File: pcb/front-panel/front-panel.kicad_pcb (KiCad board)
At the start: 2 copper layers, 99.1 x 19 mm, 5 parts, among them J1 HEADER-1x05, U1 ER-OLED1602-4W, U2 TSL2561

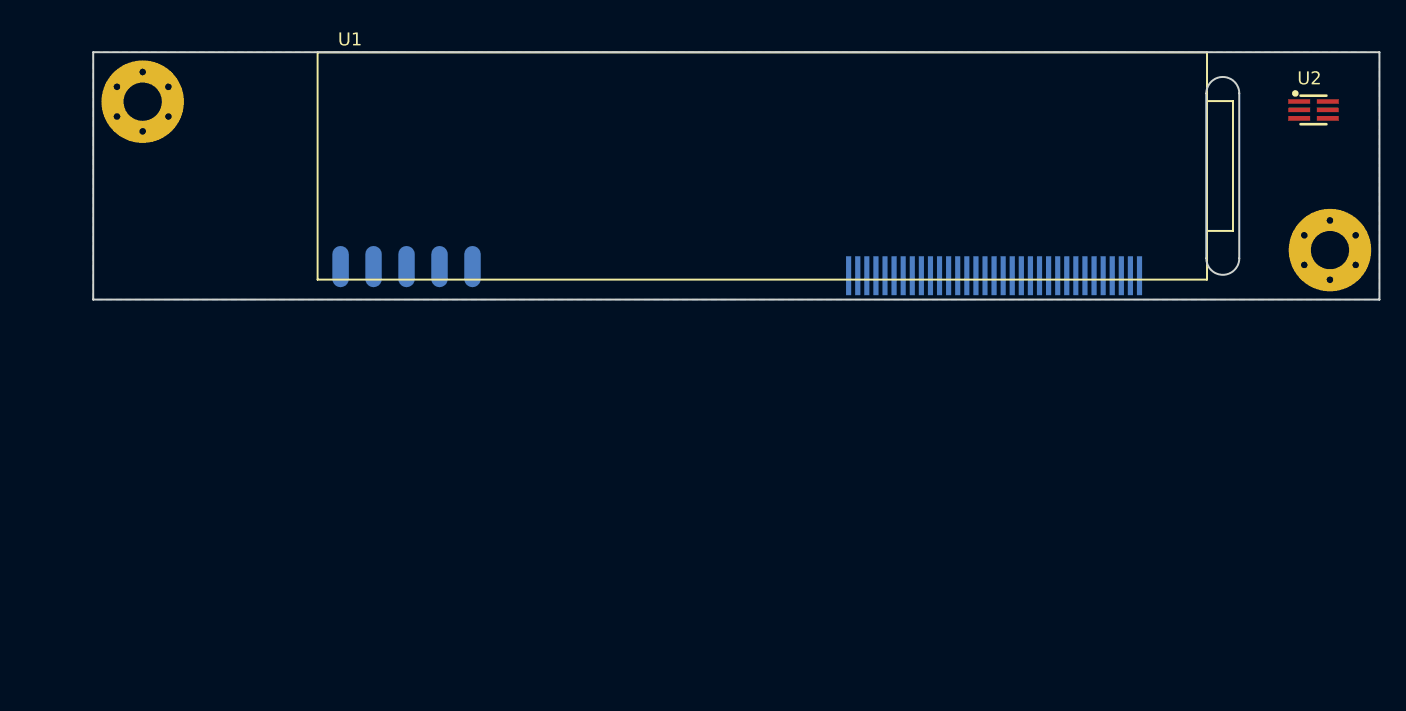
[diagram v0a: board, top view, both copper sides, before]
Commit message: Added schematic for front panel pcb
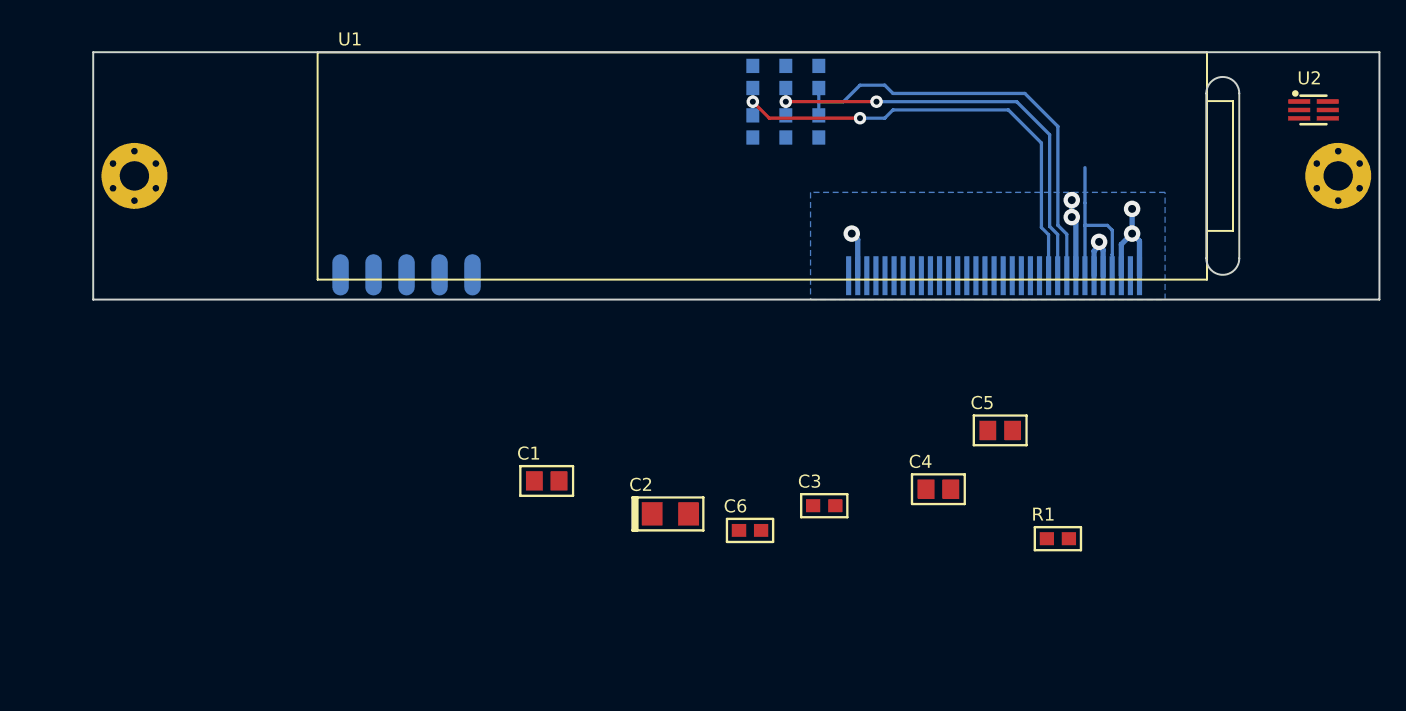
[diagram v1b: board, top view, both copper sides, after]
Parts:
- removed REF (x2): Hole-Screw-#4, Conn-Wire-Pads:Hole-Screw-#4
- added C1: 1uF, SMT:C-0805, F.Cu at (129.5, 128.3)
- added C2: 4.7uF, SMT:CPL-1206, F.Cu at (139.1, 130.8)
- added C3: 100nF, SMT:C-0603, F.Cu at (150.9, 130.2)
- added C4: 10uF, SMT:C-0805, F.Cu at (159.7, 128.9)
- added C5: 10uF, SMT:C-0805, F.Cu at (164.5, 124.4)
- added C6: 100nF, SMT:C-0603, F.Cu at (145.2, 132.1)
- added H1: Hole, Conn-Wire-Pads:Hole-Screw-#2, F.Cu at (190.5, 104.8)
- added H2: Hole, Conn-Wire-Pads:Hole-Screw-#2, F.Cu at (97.8, 104.8)
- added R1: 500k, SMT:R-0603, F.Cu at (168.9, 132.7)
- added R2: N/A, SMT:R-0603, B.Cu at (150.5, 97.2)
- added R3: 0, SMT:R-0603, B.Cu at (150.5, 101.0)
- added R4: 0, SMT:R-0603, B.Cu at (148.0, 97.2)
- added R5: N/A, SMT:R-0603, B.Cu at (148.0, 101.0)
- added R6: N/A, SMT:R-0603, B.Cu at (145.4, 97.2)
- added R7: 0, SMT:R-0603, B.Cu at (145.4, 101.0)
- moved J1 0.63 mm to (118.7, 112.4)
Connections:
- net Net-(U1-Pad12) renamed /VCC_EN
- J1 pad 1: +3V3 -> +5V
- U1 pad 10: +3V3 -> Net-(R4-Pad2)
- U1 pad 11: GND -> Net-(R6-Pad2)
- U1 pad 14: Net-(U1-Pad14) -> /RESET
- U1 pad 32: Net-(U1-Pad32) -> +12V
- U1 pad 4: Net-(U1-Pad4) -> Net-(C1-Pad2)
- U1 pad 5: Net-(U1-Pad5) -> +5V
- U1 pad 6: +3V3 -> +5V
- U1 pad 7: Net-(U1-Pad7) -> Net-(C1-Pad2)
- U1 pad 8: Net-(U1-Pad8) -> +5V
- U1 pad 9: GND -> Net-(R2-Pad2)
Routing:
- net Net-(R6-Pad2): track 0.00 -> 36.6 mm, vias 0 -> 2
- net Net-(R4-Pad2): track 0.00 -> 34.6 mm, vias 0 -> 2
- net Net-(R2-Pad2): track 0.00 -> 34.1 mm
- net Net-(C1-Pad2): track 0.00 -> 14.1 mm
- net +5V: track 0.00 -> 11.1 mm, vias 0 -> 3
- net GND: track 0.00 -> 8.97 mm, vias 0 -> 2
- net +12V: track 0.00 -> 3.43 mm, vias 0 -> 1
- added copper zone on Power, net +5V
- added copper zone on GND, net GND
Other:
- copper layers 2 -> 4
- net class Default: clearance 0.2 -> 0.254; trace_width 0.25 -> 0.254; via_dia 0.6 -> 0.9652; via_drill 0.4 -> 0.4572
- net class Power added: clearance 0.254, trace_width 0.4064, via_dia 1.27, via_drill 0.6096
- rule trace_clearance: 0.2 -> 0.254

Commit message: Added front panel pcb
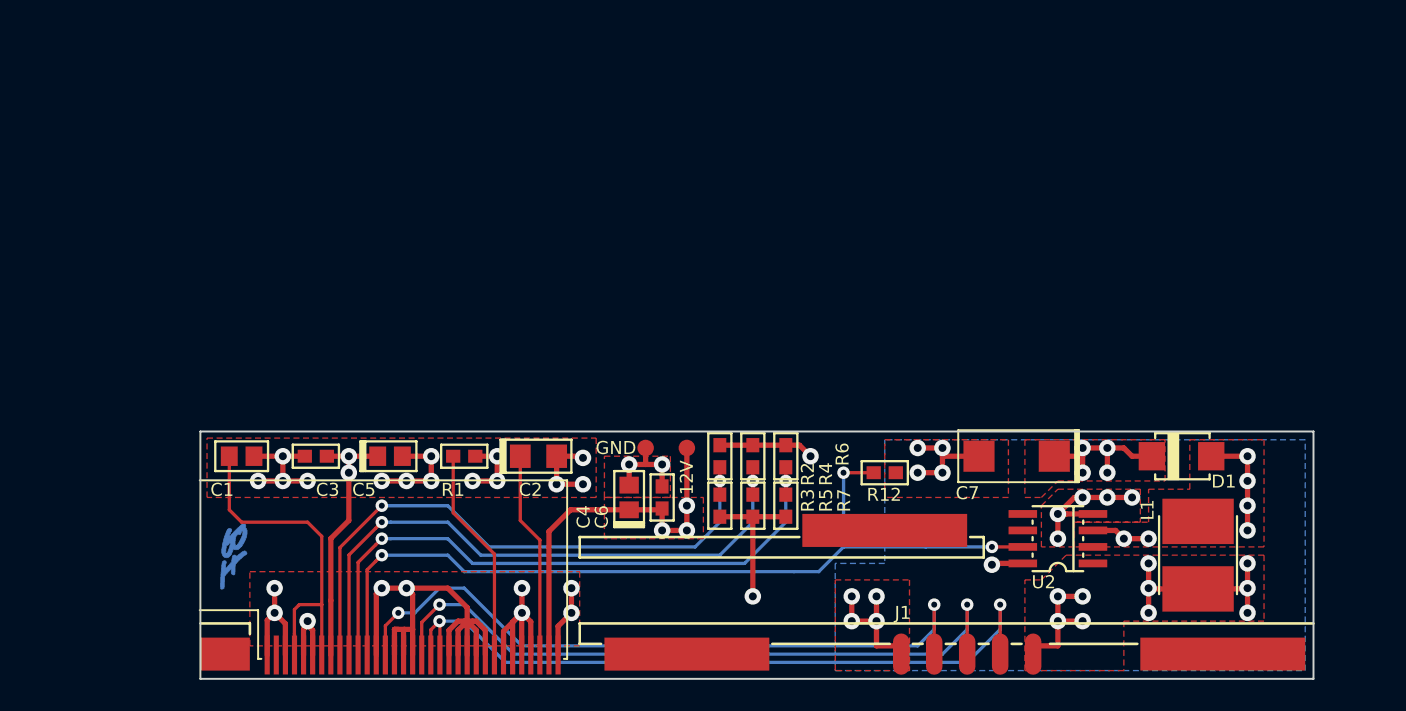
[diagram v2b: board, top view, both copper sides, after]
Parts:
- removed H1, H2: Hole, Conn-Wire-Pads:Hole-Screw-#2
- added C7: 22uF, SMT:CPL-2312, F.Cu at (165.7, 126.4)
- added D1: MBRS120T3, SMT:DO-214-AA, F.Cu at (178.4, 126.4)
- added J2: HEADER-1x01, Conn-Wire-Pads:SolderPad-100x500, F.Cu at (181.6, 141.6)
- added J3: HEADER-1x01, Conn-Wire-Pads:SolderPad-100x500, F.Cu at (140.3, 141.6)
- added J4: HEADER-1x01, Conn-Wire-Pads:SolderPad-100x500, F.Cu at (155.6, 132.1)
- added J5: HEADER-1x01, Conn-Wire-Pads:SolderPad-100x150, F.Cu at (104.8, 141.6)
- added L1: 33uH, SMT:IND-CD54, F.Cu at (179.7, 134.0)
- added R12: 10k, SMT:R-0603, F.Cu at (155.6, 127.6)
- added REF**: VAL**, Symbols:Gauge-X-100mm, B.Cu at (96.5, 143.5)
- added REF**: VAL**, Symbols:SIGNATURE, B.Cu at (105.4, 134.0)
- added REF**: VAL**, Symbols:LOGO-OSHW-150, B.Cu at (179.3, 127.6)
- added REF**: VAL**, Symbols:Gauge-X-100mm, F.Cu at (102.9, 149.9)
- added TP1: 12V, Conn-Wire-Pads:TEST-POINT-50, F.Cu at (140.3, 125.7)
- added TP2: GND, Conn-Wire-Pads:TEST-POINT-50, F.Cu at (137.2, 125.7)
- C4, C5: footprint SMT:C-0805 -> SMT:CPL-0805
- J1, R3, R4, R7: moved to F.Cu
- R2, R5, R6: value N/A -> DNP; moved to F.Cu
- U1: moved to B.Cu
- U2: value TSL2561 -> LT1109CS8-12; footprint SMT-DFN:6 -> SMT-SOIC:SOIC8
- moved J1 52.1 mm to (161.9, 141.6), turned to 180 degrees
- moved C5 47.0 mm to (117.5, 126.4)
- moved R1 46.2 mm to (123.2, 126.4)
- moved C3 39.3 mm to (111.8, 126.4)
- moved U2 38.4 mm to (168.9, 132.7), turned to 90 degrees
- moved R3 30.2 mm to (142.9, 130.2)
- moved R2 30.2 mm to (142.9, 126.4)
- moved U1 29.6 mm to (139.1, 133.2), turned to 180 degrees
- moved R5 29.3 mm to (145.4, 130.2)
- moved R7 29.3 mm to (148.0, 130.2)
- moved R4 29.3 mm to (145.4, 126.4)
- moved R6 29.3 mm to (148.0, 126.4)
- moved C4 23.8 mm to (135.9, 129.5), turned to 90 degrees
- moved C1 23.6 mm to (106.0, 126.4), turned to 180 degrees
- moved C2 11.1 mm to (128.9, 126.4)
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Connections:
- U1 pad 15: (no net) -> GND
- U2 pad 1: (no net) -> +5V
- U2 pad 2: (no net) -> Net-(U2-Pad2)
- U2 pad 3: (no net) -> /SW_12V
- U2 pad 4: (no net) -> GND
- U2 pad 5: (no net) -> Net-(U2-Pad5)
- U2 pad 6: (no net) -> Net-(U2-Pad6)
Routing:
- net GND: track 8.97 -> 148.0 mm, vias 2 -> 38
- net /VCC_EN: track 0.00 -> 66.9 mm, vias 0 -> 3
- net /SDA: track 0.00 -> 56.1 mm, vias 0 -> 2
- net +12V: track 3.43 -> 56.8 mm, vias 1 -> 8
- net /RESET: track 0.00 -> 53.2 mm, vias 0 -> 2
- net /SCL: track 0.00 -> 52.5 mm, vias 0 -> 2
- net +5V: track 11.1 -> 57.1 mm, vias 3 -> 14
- net Net-(R1-Pad1): track 0.00 -> 16.6 mm
- net Net-(C2-PadA): track 0.00 -> 15.9 mm
- net /SW_12V: track 0.00 -> 13.1 mm, vias 0 -> 6
- net Net-(C1-Pad2): track 14.1 -> 27.0 mm
- net Net-(R4-Pad2): track 34.6 -> 47.2 mm
- net Net-(R2-Pad2): track 34.1 -> 46.3 mm, vias 0 -> 2
- net Net-(R6-Pad2): track 36.6 -> 48.2 mm
- added copper zone on F.Cu, net +12V
- added copper zone on Power, net +12V
- added copper zone on F.Cu, net +5V
- added copper zone on F.Cu, net /SW_12V
- added copper zone on Power, net /SW_12V
- added copper zone on F.Cu, net GND
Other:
- board size 99.1 x 19 mm -> 85.7 x 19 mm
- board text added: "PC-04"
- board text added: "REV. A"

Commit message: EN of 12V suply controlled from MCU instead of LCD GPIO
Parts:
- J1: value HEADER-1x05 -> HEADER-1x06; footprint Conn-Wire-Pads:WP-50mil-1x05 -> Conn-Wire-Pads:WP-50mil-1x06
- moved J1 1.42 mm to (160.7, 141.0)
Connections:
- J1 pad 5: GND -> /VCC_EN
- U1 pad 12: /VCC_EN -> Net-(U1-Pad12)
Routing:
- net /VCC_EN: track 66.9 -> 28.0 mm

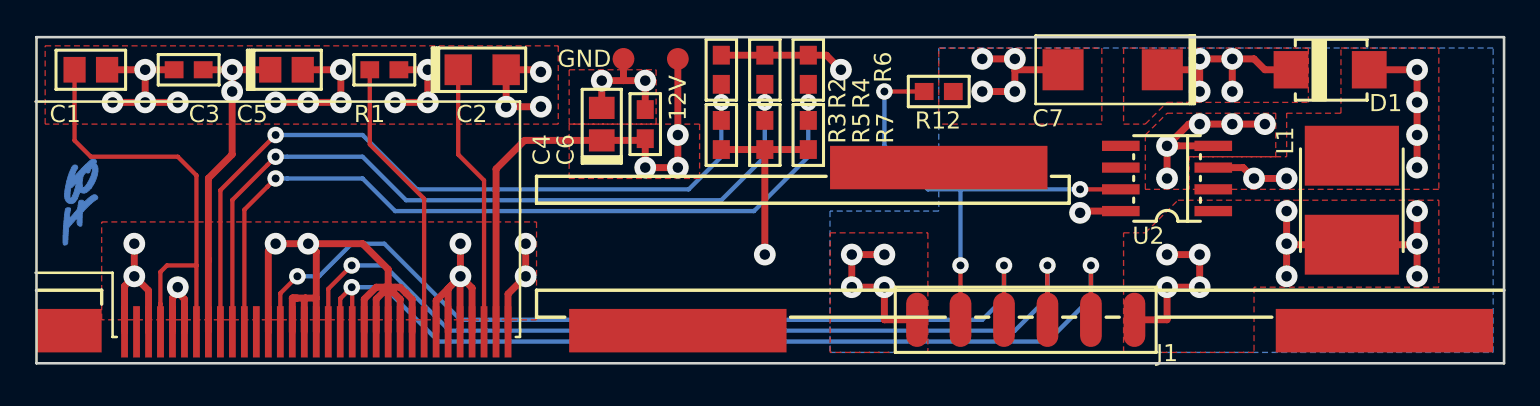
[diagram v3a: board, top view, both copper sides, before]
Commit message: Changed touch keypad, front panel and light sensor pcb to a two layer design.
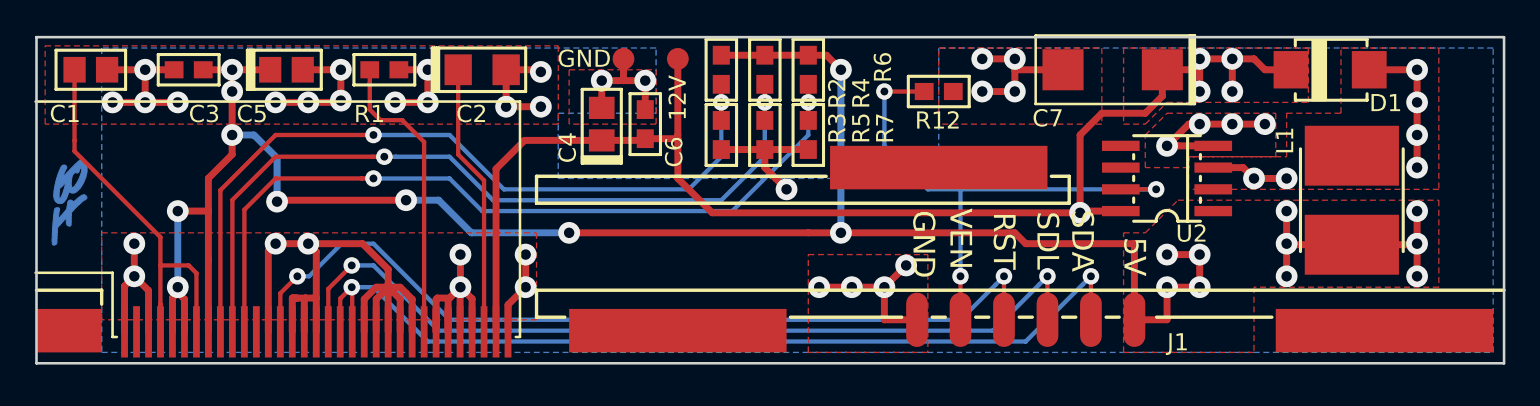
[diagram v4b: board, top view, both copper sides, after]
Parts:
- moved REF** 0.63 mm to (104.8, 134.0)
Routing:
- net +5V: track 57.1 -> 134.2 mm, vias 14 -> 20
- net +12V: track 56.8 -> 78.0 mm, vias 8 -> 5
- net GND: track 148.0 -> 142.6 mm, vias 38 -> 37
- net /VCC_EN: track 28.0 -> 32.1 mm
- net Net-(C1-Pad2): track 27.0 -> 23.1 mm
- net /SDA: track 56.1 -> 54.1 mm
- net /SCL: track 52.5 -> 50.5 mm
- net /RESET: track 53.2 -> 51.2 mm
- net Net-(R1-Pad1): track 16.6 -> 17.4 mm
- net Net-(R6-Pad2): track 48.2 -> 47.5 mm
- removed copper zone on Power, net +12V
- removed copper zone on Power, net +5V
- removed copper zone on Power, net /SW_12V
- removed copper zone on GND, net GND
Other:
- copper layers 4 -> 2
- board text added: "5V"
- board text added: "GND"
- board text added: "RST"
- board text added: "SDA"
- board text added: "SDL"
- board text added: "VEN"

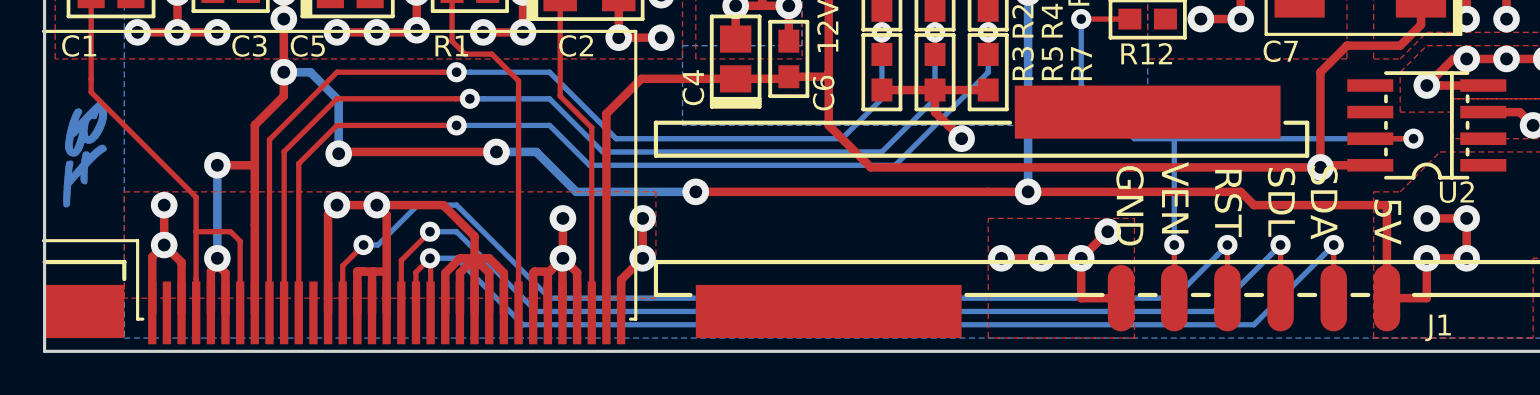
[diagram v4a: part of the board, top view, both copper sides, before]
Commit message: Added pull down resistor to Reset line.
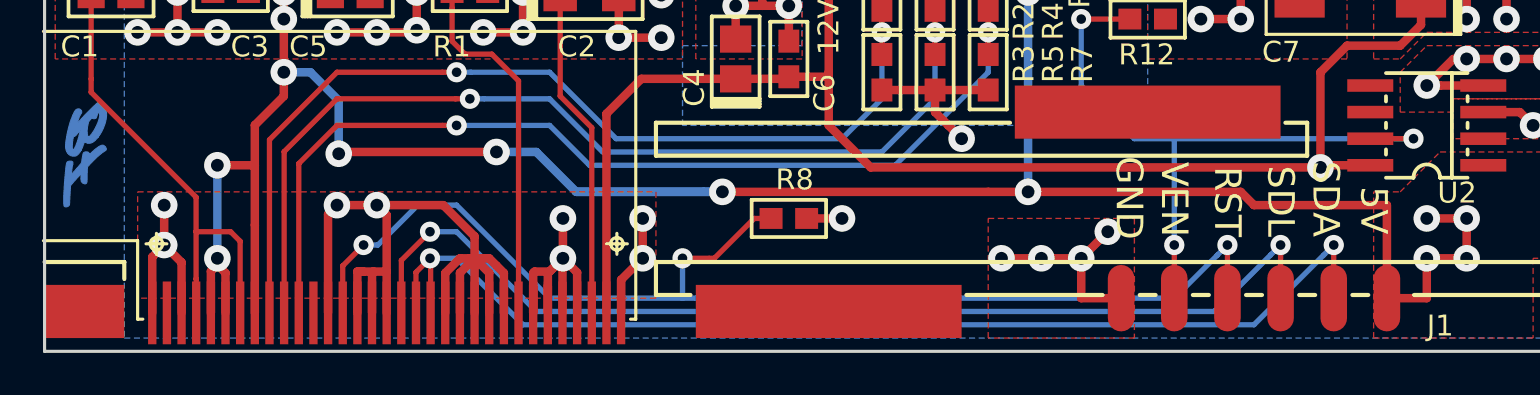
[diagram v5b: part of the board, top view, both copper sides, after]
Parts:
- added R8: 10k, SMT:R-0603, F.Cu at (138.4, 137.2)
- R1: value 500k -> 470k
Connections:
- net /RESET renamed /~RESET
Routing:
- net +5V: track 134.2 -> 141.2 mm
- net /~RESET: track 51.2 -> 58.1 mm, vias 2 -> 3
- net GND: track 142.6 -> 144.2 mm, vias 37 -> 38
